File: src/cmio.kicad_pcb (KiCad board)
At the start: 2 copper layers, 89 x 51 mm, 30 parts, among them J1 CONN_01X02_MALE, J2 CONN_02X20, J3 USB_OTG, J4 CM3Lite, J5 CONN_COAXIAL, J6 CONN_02X20, J7 Micro_SD_Card_TFP09_2_12B, J8 CONN_01X06, J9 USB_OTG, SW1 SW_Push, U1 ISL91107IR, U2 LD3985M18R, U3 LD3985M28R

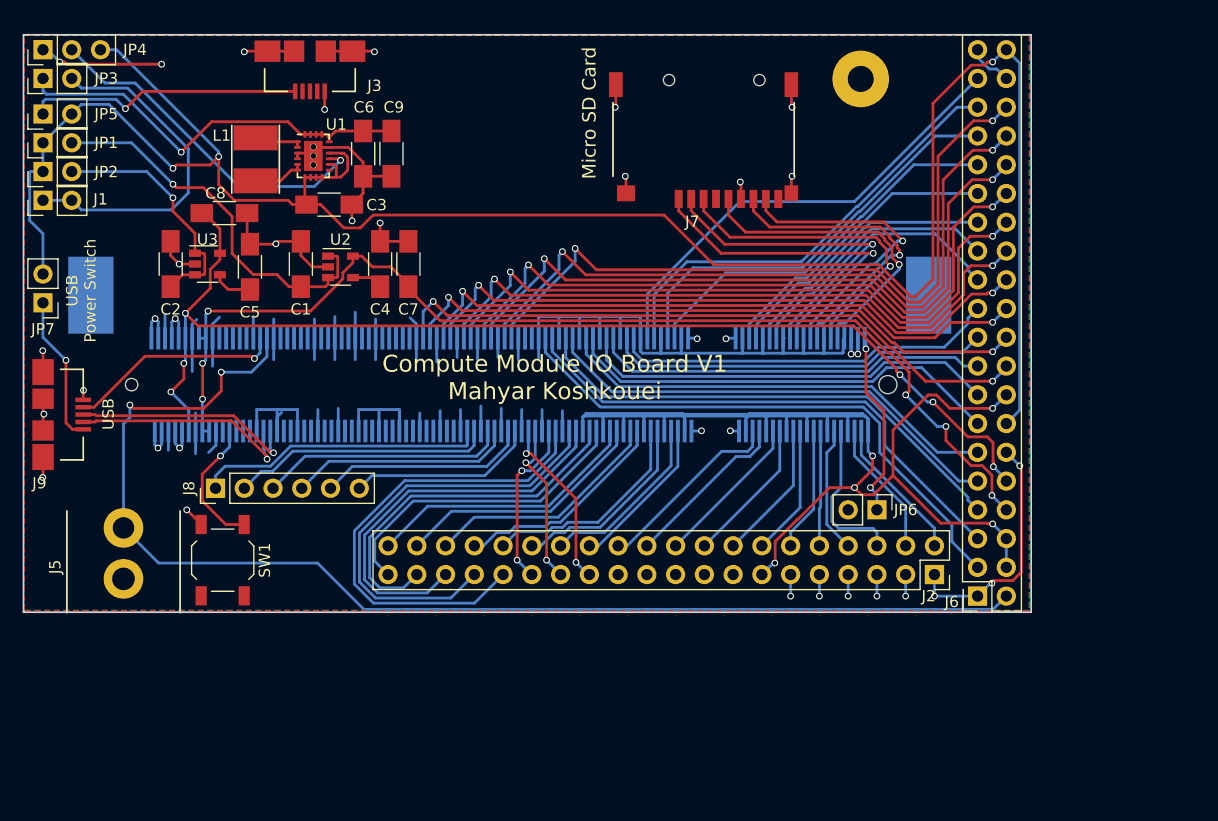
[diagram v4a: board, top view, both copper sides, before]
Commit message: Many changes
Added pull downs to the four GPIO pins that do not have a pull down or
pull up integrated.
Using surface mount pin sockets to reduce PCB space.
Using copper fills for some power tracks.
Using thicker tracks for power.
Added decoupling capacitor close to SD card.
Modified DDR2 footprint to the module that I have - TE SODIMM SOCKET 1473149-4.

Signed-off-by: Mahyar Koshkouei <deltabeard@users.noreply.github.com>
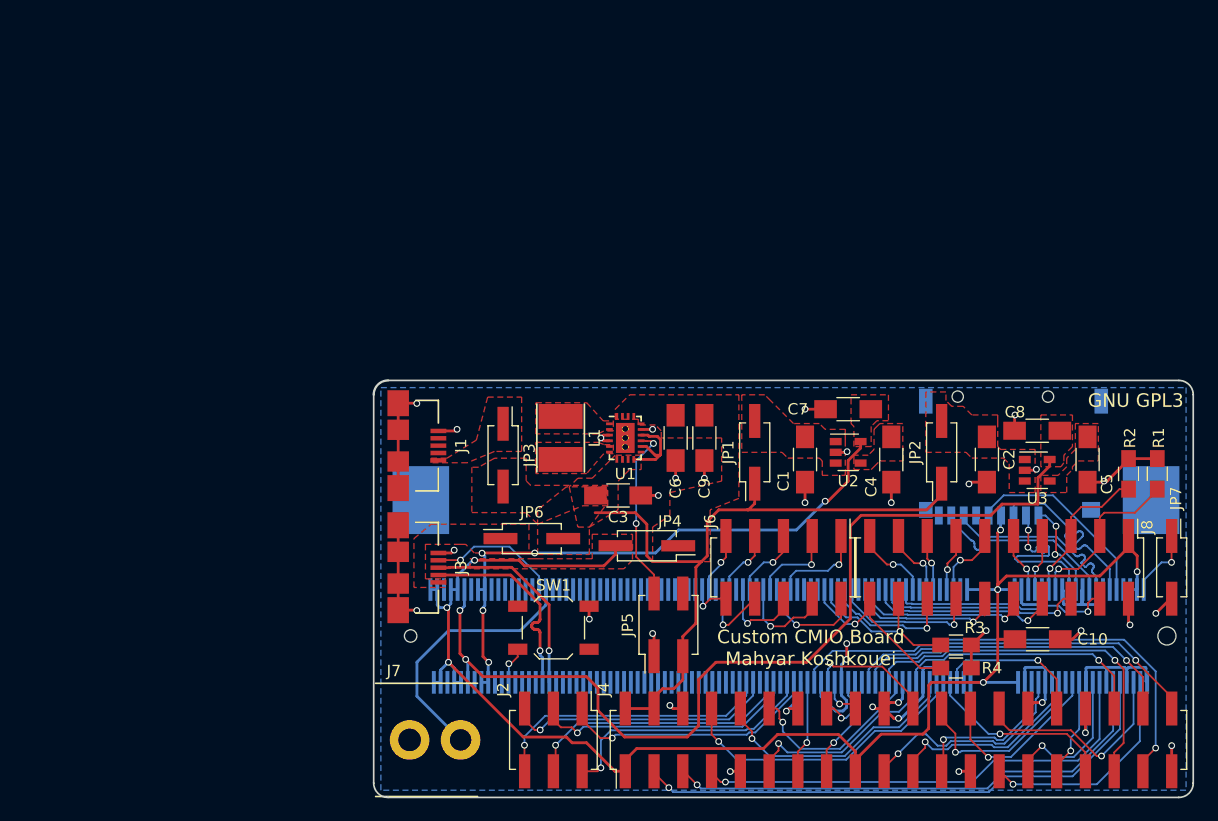
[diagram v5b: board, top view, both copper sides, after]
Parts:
- added C10: 4.7uF, Capacitors_SMD:C_1206_HandSoldering, F.Cu at (133.6, 72.4)
- added R1: 100K, Resistors_SMD:R_0805_HandSoldering, F.Cu at (144.1, 57.8)
- added R2: 100K, Resistors_SMD:R_0805_HandSoldering, F.Cu at (141.6, 57.8)
- added R3: 100K, Resistors_SMD:R_0805_HandSoldering, F.Cu at (126.4, 72.9)
- added R4: 100K, Resistors_SMD:R_0805_HandSoldering, F.Cu at (126.4, 74.9)
- J1: value CONN_01X02_MALE -> USB_OTG; footprint Pin_Headers:Pin_Header_Straight_1x02_Pitch2.54mm -> foot:Micro_USB_B_10104110
- J2: value CONN_02X20 -> BANK0; footprint Socket_Strips:Socket_Strip_Straight_2x20_Pitch2.54mm -> Pin_Headers:Pin_Header_Straight_2x20_Pitch2.54mm_SMD
- J4: value CM3Lite -> DSI0; footprint foot:CM3_LeftDrillHole_Socket_SODIMM_DDR1-2_TE_1612618 -> Pin_Headers:Pin_Header_Straight_2x03_Pitch2.54mm_SMD; moved to F.Cu
- J5: value CONN_COAXIAL -> CM3Lite; footprint foot:RCA_PHONO -> foot:Socket_SODIMM_DDR1-2_TE_1612618; moved to B.Cu
- J6: value CONN_02X20 -> DSI1; footprint Socket_Strips:Socket_Strip_Straight_2x20_Pitch2.54mm -> Pin_Headers:Pin_Header_Straight_2x05_Pitch2.54mm_SMD
- J7: value Micro_SD_Card_TFP09_2_12B -> TVOUT; footprint foot:TFP09-2-12B -> foot:RCA_PHONO
- J8: value CONN_01X06 -> BANK1; footprint Pin_Headers:Pin_Header_Straight_1x06_Pitch2.54mm -> Pin_Headers:Pin_Header_Straight_2x10_Pitch2.54mm_SMD
- J9: value USB_OTG -> Micro_SD_Card_TFP09_2_12B; footprint foot:Micro_USB_B_10104110 -> foot:TFP09-2-12B; moved to B.Cu
- JP1, JP2: footprint Pin_Headers:Pin_Header_Straight_1x02_Pitch2.54mm -> Pin_Headers:Pin_Header_Straight_2x01_Pitch2.54mm_SMD
- JP3: value 3.3 OUT -> TP; footprint Pin_Headers:Pin_Header_Straight_1x02_Pitch2.54mm -> Pin_Headers:Pin_Header_Straight_2x01_Pitch2.54mm_SMD
- JP4: value EN_Jumper -> 3.3 OUT; footprint Socket_Strips:Socket_Strip_Straight_1x03_Pitch2.54mm -> Pin_Headers:Pin_Header_Straight_2x01_Pitch2.54mm_SMD
- JP5: value TP -> EN_Jumper; footprint Pin_Headers:Pin_Header_Straight_1x02_Pitch2.54mm -> Pin_Headers:Pin_Header_Straight_2x02_Pitch2.54mm_SMD
- JP6: value Disable SD Card -> PWRUSB; footprint Pin_Headers:Pin_Header_Straight_1x02_Pitch2.54mm -> Pin_Headers:Pin_Header_Straight_2x01_Pitch2.54mm_SMD
- JP7: value PWRUSB -> Disable SD Card; footprint Pin_Headers:Pin_Header_Straight_1x02_Pitch2.54mm -> Pin_Headers:Pin_Header_Straight_2x01_Pitch2.54mm_SMD
- SW1: value SW_Push -> Reset
- moved JP7 102.4 mm to (145.4, 66.0), turned to 270 degrees
- moved JP2 83.2 mm to (125.1, 55.9)
- moved J9 82.6 mm to (131.4, 61.0), turned to 0 degrees
- moved C5 75.9 mm to (138.0, 56.5), turned to 270 degrees
- moved U3 75.5 mm to (133.5, 57.5)
- moved C8 74.3 mm to (133.5, 54.0), turned to 180 degrees
- moved C2 74.1 mm to (129.1, 56.5), turned to 270 degrees
- moved JP5 71.3 mm to (101.0, 71.1)
- moved J8 69.6 mm to (130.2, 66.0), turned to 270 degrees
- moved JP4 69.0 mm to (99.1, 64.1), turned to 180 degrees
- moved JP1 68.6 mm to (108.6, 55.9)
- moved J5 59.0 mm to (111.6, 72.1), turned to 180 degrees
- moved J7 54.8 mm to (78.1, 81.3), turned to 0 degrees
- moved JP3 52.5 mm to (86.4, 56.1), turned to 270 degrees
- moved C4 48.3 mm to (120.7, 56.5), turned to 270 degrees
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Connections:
- J1 pad 1: +3V3 -> Net-(J1-Pad1)
- J1 pad 2: +3V3 -> (no net)
- J2 pad 10: /G4 -> /BCM_15
- J2 pad 11: +3V3 -> /BCM_17
- J2 pad 12: /G5 -> /BCM_18
- J2 pad 13: GND -> /BCM_27
- J2 pad 14: /G6 -> GND
- J2 pad 15: GND -> /BCM_22
- J2 pad 16: /G7 -> /BCM_23
- J2 pad 17: GND -> +3V3
- J2 pad 18: /G8 -> /BCM_24
- J2 pad 19: GND -> /BCM_10
- J2 pad 2: /G0 -> +5V
- J2 pad 20: /G9 -> GND
- J2 pad 21: GND -> /BCM_9
- J2 pad 22: /G10 -> /BCM_25
- J2 pad 23: GND -> /BCM_11
- J2 pad 24: /G11 -> /BCM_8
- J2 pad 25: /G27 -> GND
- J2 pad 26: /G12 -> /BCM_7
- J2 pad 27: /G26 -> /BCM_0
- J2 pad 28: /G13 -> /BCM_1
- J2 pad 29: /G25 -> /BCM_5
- J2 pad 3: +3V3 -> /BCM_2
- J2 pad 30: /G14 -> GND
- J2 pad 31: /G24 -> /BCM_6
- J2 pad 32: /G15 -> /BCM_12
- J2 pad 33: /G23 -> /BCM_13
- J2 pad 34: /G16 -> GND
- J2 pad 35: /G22 -> /BCM_19
- J2 pad 36: /G17 -> /BCM_16
- J2 pad 37: /G21 -> /BCM_26
- J2 pad 38: /G18 -> /BCM_20
- J2 pad 39: /G20 -> GND
- J2 pad 4: /G1 -> +5V
- J2 pad 40: /G19 -> /BCM_21
- J2 pad 5: +3V3 -> /BCM_3
- J2 pad 6: /G2 -> GND
- J2 pad 7: +3V3 -> /BCM_4
- J2 pad 8: /G3 -> /BCM_14
- J2 pad 9: +3V3 -> GND
- J3 pad 2: (no net) -> /D-
- J3 pad 3: (no net) -> /D+
- J3 pad 4: (no net) -> OTDIG
- J4 pad 1: GND -> /DSI0_0
- J4 pad 2: Net-(J4-Pad2) -> /DSI0_1
- J4 pad 3: /G0 -> /DSI0_2
- J4 pad 4: +3V3 -> /DSI0_3
- J4 pad 5: /G1 -> /DSI0_4
- J4 pad 6: +3V3 -> /DSI0_5
- J5 pad 1: TVDAC -> GND
- J5 pad 2: GND -> Net-(J5-Pad2)
- J6 pad 1: +3V3 -> /DSI1_0
- J6 pad 10: +2V8 -> /DSI1_9
- J6 pad 2: TVDAC -> /DSI1_1
- J6 pad 3: /G45 -> /DSI1_2
- J6 pad 4: GND -> /DSI1_3
- J6 pad 5: /G44 -> /DSI1_4
- J6 pad 6: GND -> /DSI1_5
- J6 pad 7: /G43 -> /DSI1_6
- J6 pad 8: +1V8 -> /DSI1_7
- J6 pad 9: /G42 -> /DSI1_8
- J7 pad 1: DAT2 -> TVDAC
- J7 pad 2: DAT3 -> GND
- J8 pad 1: /DSI0_5 -> +3V3
- J8 pad 2: /DSI0_4 -> GND
- J8 pad 3: /DSI0_3 -> /BCM_28
- J8 pad 4: /DSI0_2 -> /BCM_37
- J8 pad 5: /DSI0_1 -> /BCM_29
- J8 pad 6: /DSI0_0 -> /BCM_38
- J9 pad 1: Net-(J9-Pad1) -> DAT2
- J9 pad 2: /D- -> DAT3
- J9 pad 3: /D+ -> CMD
- J9 pad 4: OTDIG -> +3V3
- J9 pad 5: GND -> CLK
- JP3 pad 1: Net-(C6-Pad2) -> Net-(J1-Pad1)
- JP3 pad 2: +3V3 -> +5V
- JP4 pad 1: GND -> Net-(C6-Pad2)
- JP4 pad 2: Net-(JP4-Pad2) -> +3V3
- JP5 pad 1: Net-(J3-Pad1) -> GND
- JP5 pad 2: +5V -> Net-(JP5-Pad2)
- JP6 pad 1: Net-(J4-Pad2) -> Net-(J3-Pad1)
- JP6 pad 2: GND -> +5V
- JP7 pad 1: Net-(J9-Pad1) -> Net-(J5-Pad2)
- JP7 pad 2: +5V -> GND
- SW1 pad 2: Net-(J4-Pad177) -> Net-(J5-Pad177)
- U1 pad 13: Net-(JP4-Pad2) -> Net-(JP5-Pad2)
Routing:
- net GND: track 341.8 -> 132.3 mm, vias 24 -> 35
- net +5V: track 187.9 -> 67.4 mm, vias 3 -> 0
- net TVDAC: track 109.3 -> 23.3 mm, vias 2 -> 0
- net +3V3: track 82.0 -> 139.4 mm, vias 18 -> 7
- net /DSI1_0: track 64.1 -> 8.47 mm, vias 2 -> 1
- net /DSI1_9: track 57.8 -> 3.80 mm, vias 2 -> 1
- net /DSI1_2: track 61.6 -> 7.80 mm, vias 2 -> 1
- net /DSI1_1: track 62.8 -> 9.64 mm, vias 2 -> 1
- net /DSI1_4: track 58.9 -> 6.44 mm, vias 2 -> 1
- net /DSI1_8: track 56.1 -> 5.35 mm, vias 2 -> 1
- net /DSI1_3: track 60.0 -> 9.81 mm, vias 2 -> 1
- net /DSI1_6: track 56.0 -> 5.90 mm, vias 2 -> 1
- net /G45: track 49.7 -> 0.00 mm
- net /DSI1_5: track 57.3 -> 7.89 mm, vias 2 -> 1
- net /DSI1_7: track 55.6 -> 6.89 mm, vias 2 -> 1
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- added copper zone on F.Cu, net +1V8
- added copper zone on F.Cu, net +2V8
- added copper zone on F.Cu, net +5V
- added copper zone on F.Cu, net Net-(C1-Pad1)
- added copper zone on F.Cu, net Net-(C2-Pad1)
- added copper zone on F.Cu, net Net-(C4-Pad1)
- added copper zone on F.Cu, net Net-(C5-Pad1)
- added copper zone on F.Cu, net Net-(C6-Pad2)
- added copper zone on F.Cu, net Net-(J1-Pad1)
- added copper zone on F.Cu, net Net-(J3-Pad1)
- added copper zone on F.Cu, net Net-(L1-Pad1)
- added copper zone on F.Cu, net Net-(L1-Pad2)
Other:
- board size 89 x 51 mm -> 72.4 x 36.8 mm
- net class Default: clearance 0.2 -> 0.16; trace_width 0.25 -> 0.16
- net class PWR added: clearance 0.2, trace_width 0.25, via_dia 0.6, via_drill 0.4
- rule trace_clearance: 0.2 -> 0.16
- rule trace_min: 0.2 -> 0.15
- board text added: "Custom CMIO Board Mahyar Koshkouei"
- board text added: "GNU GPL3"
- board text added: "Micro SD"
- board text added: "Raspberry Pi Compute Module"
- board text removed: "Compute Module IO Board V1 Mahyar Koshkouei"
- board text removed: "Micro SD Card"
- board text removed: "USB"
- board text removed: "USB Power Switch"

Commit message: Minor changes that I can't remember
Signed-off-by: Mahyar Koshkouei <deltabeard@users.noreply.github.com>
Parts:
- moved J7 0.64 mm to (77.5, 81.3)
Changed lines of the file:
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@@
     (last_trace_width 0.16)
     (trace_clearance 0.16)
-    (zone_clearance 0.25)
+    (zone_clearance 0.5)
     (zone_45_only no)
     (trace_min 0.15)
@@
     (visible_elements FFFFFF7F)
     (pcbplotparams
-      (layerselection 0x01030_ffffffff)
+      (layerselection 0x010f0_ffffffff)
       (usegerberextensions false)
       (excludeedgelayer true)
@@
       (effects (font (size 1 1) (thickness 0.15)))
     )
-    (fp_text value 22uF (at 0 2) (layer F.Fab)
+    (fp_text value 22uF (at -2.54 1.905) (layer F.Fab)
       (effects (font (size 1 1) (thickness 0.15)))
     )
@@
   )
   (module foot:RCA_PHONO (layer F.Cu)
-    (at 78.105 81.28)
+    (at 77.47 81.28)
     (fp_text reference J7 (at -1.397 -6.096) (layer F.SilkS)
       (effects (font (size 1 1) (thickness 0.15)))
@@
   (segment (start 100.203 56.134) (end 99.829581 56.507419) (width 0.25) (layer F.Cu) (net 2))
   (segment (start 99.829581 56.507419) (end 97.905 56.507419) (width 0.25) (layer F.Cu) (net 2) (status 20))
+  (via (at 94.996 54.61) (size 0.6) (drill 0.4) (layers F.Cu B.Cu) (net 3))
+  (segment (start 95.246 54.36) (end 94.996 54.61) (width 0.25) (layer F.Cu) (net 3))
+  (segment (start 95.246 54.86) (end 94.996 54.61) (width 0.25) (layer F.Cu) (net 3))
+  (segment (start 95.755 54.36) (end 95.246 54.36) (width 0.25) (layer F.Cu) (net 3) (status 10))
+  (segment (start 95.755 54.86) (end 95.246 54.86) (width 0.25) (layer F.Cu) (net 3) (status 10))
   (segment (start 141.605 56.435) (end 141.605 56.535) (width 0.25) (layer F.Cu) (net 3))
   (segment (start 139.72 58.42) (end 139.446 58.42) (width 0.25) (layer F.Cu) (net 3))
@@
   (segment (start 132.44 57.465) (end 133.381102 57.465) (width 0.25) (layer F.Cu) (net 3) (status 10))
   (via (at 133.464546 57.381556) (size 0.6) (drill 0.4) (layers F.Cu B.Cu) (net 3))
-  (segment (start 95.755 54.36) (end 95.246 54.36) (width 0.25) (layer F.Cu) (net 3) (status 10))
-  (segment (start 95.246 54.36) (end 94.996 54.61) (width 0.25) (layer F.Cu) (net 3))
-  (segment (start 95.755 54.86) (end 95.246 54.86) (width 0.25) (layer F.Cu) (net 3) (status 10))
-  (via (at 94.996 54.61) (size 0.6) (drill 0.4) (layers F.Cu B.Cu) (net 3))
-  (segment (start 95.246 54.86) (end 94.996 54.61) (width 0.25) (layer F.Cu) (net 3))
   (segment (start 145.415 68.81) (end 145.312 68.81) (width 0.25) (layer F.Cu) (net 3) (status 30))
   (segment (start 145.312 68.81) (end 144.018 70.104) (width 0.25) (layer F.Cu) (net 3) (status 10))
@@
   (segment (start 104.672 68.81) (end 104.013 69.469) (width 0.16) (layer F.Cu) (net 21))
   (via (at 104.013 69.469) (size 0.6) (drill 0.4) (layers F.Cu B.Cu) (net 21))
-  (segment (start 90.145 68) (end 90.145 69.367) (width 0.25) (layer B.Cu) (net 22) (status 10))
+  (segment (start 90.145 68) (end 90.145 69.367) (width 0.25) (layer B.Cu) (net 22))
   (segment (start 90.145 69.367) (end 87.884 71.628) (width 0.25) (layer B.Cu) (net 22))
+  (segment (start 78.75 78.06) (end 81.97 81.28) (width 0.25) (layer B.Cu) (net 22))
   (segment (start 87.884 71.628) (end 81.534 71.628) (width 0.25) (layer B.Cu) (net 22))
   (segment (start 81.534 71.628) (end 78.75 74.412) (width 0.25) (layer B.Cu) (net 22))
-  (segment (start 78.75 74.412) (end 78.75 77.425) (width 0.25) (layer B.Cu) (net 22))
-  (segment (start 78.75 77.425) (end 82.605 81.28) (width 0.25) (layer B.Cu) (net 22) (status 20))
+  (segment (start 78.75 74.412) (end 78.75 78.06) (width 0.25) (layer B.Cu) (net 22))
   (segment (start 130.575011 59.679989) (end 129.245 61.01) (width 0.16) (layer B.Cu) (net 28) (status 20))
   (segment (start 134.932552 59.679989) (end 130.575011 59.679989) (width 0.16) (layer B.Cu) (net 28))
@@
   )
   (zone (net 27) (net_name "Net-(C6-Pad2)") (layer F.Cu) (hatch edge 0.508)
-    (connect_pads (clearance 0.2))
-    (min_thickness 0.1)
+    (connect_pads (clearance 0.3))
+    (min_thickness 0.2)
     (fill yes (arc_segments 16) (thermal_gap 0.25) (thermal_bridge_width 0.5))
     (polygon
       (pts
-        (xy 107.188 59.944) (xy 104.648 60.96) (xy 104.648 65.532) (xy 99.568 65.532) (xy 99.568 62.484)
-        (xy 101.092 61.468) (xy 101.092 59.436) (xy 105.664 58.42) (xy 105.664 54.61) (xy 100.33 54.61)
+        (xy 106.68 59.69) (xy 104.14 60.96) (xy 104.14 65.532) (xy 99.568 65.532) (xy 99.568 62.484)
+        (xy 101.092 61.468) (xy 101.092 59.436) (xy 105.664 58.928) (xy 105.664 54.61) (xy 100.33 54.61)
         (xy 100.33 53.975) (xy 99.822 53.467) (xy 98.298 53.467) (xy 98.298 52.959) (xy 96.266 52.959)
-        (xy 96.266 52.07) (xy 97.536 50.8) (xy 107.188 50.8)
+        (xy 96.266 52.07) (xy 97.536 50.8) (xy 106.68 50.8)
       )
     )
@@
   )
   (zone (net 23) (net_name "Net-(C1-Pad1)") (layer F.Cu) (hatch edge 0.508)
-    (connect_pads (clearance 0.2))
+    (connect_pads (clearance 0.5))
     (min_thickness 0.2)
     (fill yes (arc_segments 16) (thermal_gap 0.25) (thermal_bridge_width 0.5))
@@
   )
   (zone (net 10) (net_name +1V8) (layer F.Cu) (hatch edge 0.508)
-    (connect_pads (clearance 0.2))
+    (connect_pads (clearance 0.5))
     (min_thickness 0.2)
     (fill yes (arc_segments 16) (thermal_gap 0.25) (thermal_bridge_width 0.5))
@@
   )
   (zone (net 25) (net_name "Net-(C4-Pad1)") (layer F.Cu) (hatch edge 0.508)
-    (connect_pads (clearance 0.2))
+    (connect_pads (clearance 0.5))
     (min_thickness 0.2)
     (fill yes (arc_segments 16) (thermal_gap 0.25) (thermal_bridge_width 0.5))
@@
   )
   (zone (net 24) (net_name "Net-(C2-Pad1)") (layer F.Cu) (hatch edge 0.508)
-    (connect_pads (clearance 0.2))
+    (connect_pads (clearance 0.5))
     (min_thickness 0.2)
     (fill yes (arc_segments 16) (thermal_gap 0.25) (thermal_bridge_width 0.5))
